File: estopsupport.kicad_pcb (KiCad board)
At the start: 2 copper layers, 65 x 35 mm, 23 parts, among them J1 ESTOP1, J2 ESTOP2, J3 CONTACTOR, J4 TAP_ESTOP, J5 5V_IN, J6 PWR, U1 PC817, U2 BTS6163D

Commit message: fix: shunt resistor value changed to datasheet recommendation
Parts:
- R4: value 10k -> 1k
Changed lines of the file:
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@@
 			)
 		)
-		(property "Value" "10k"
+		(property "Value" "1k"
 			(at 3.81 1.92 270)
 			(layer "F.Fab")

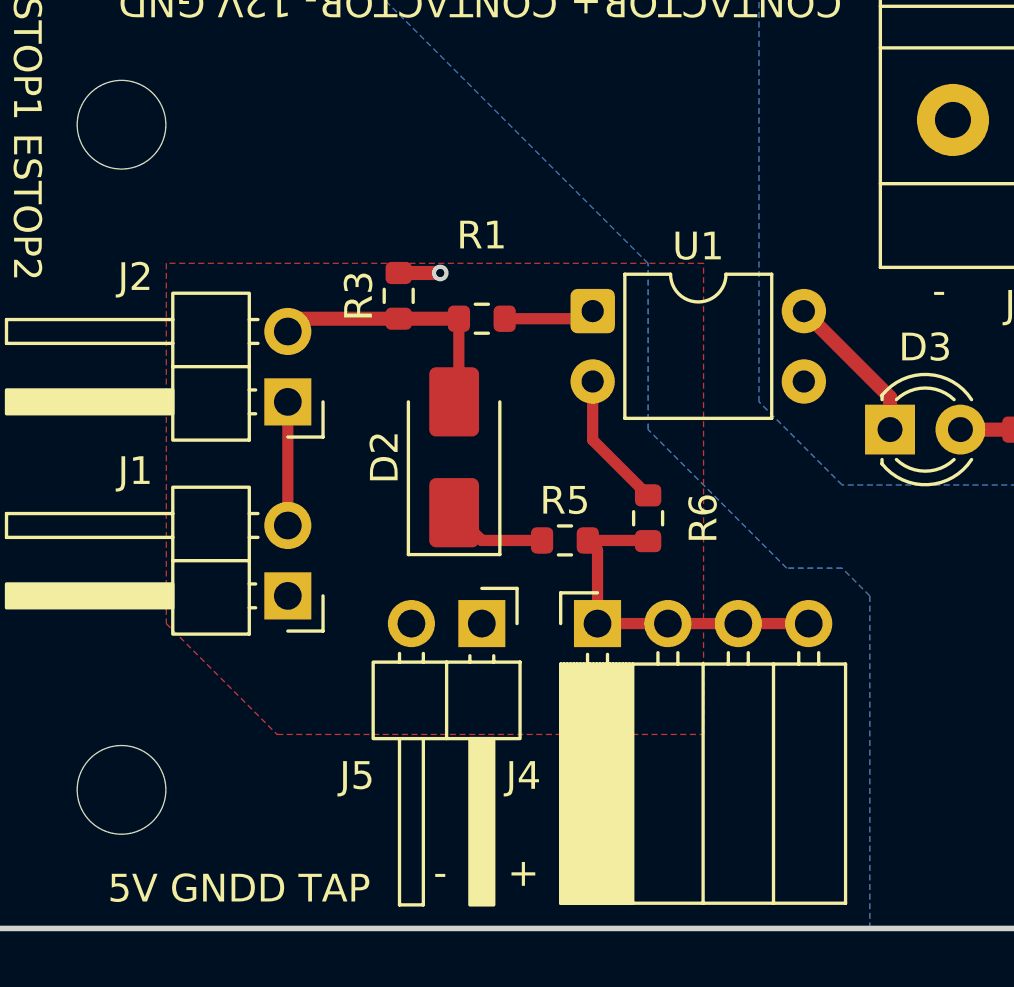
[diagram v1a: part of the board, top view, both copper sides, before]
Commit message: feat: started BOM, added ground lines to tap
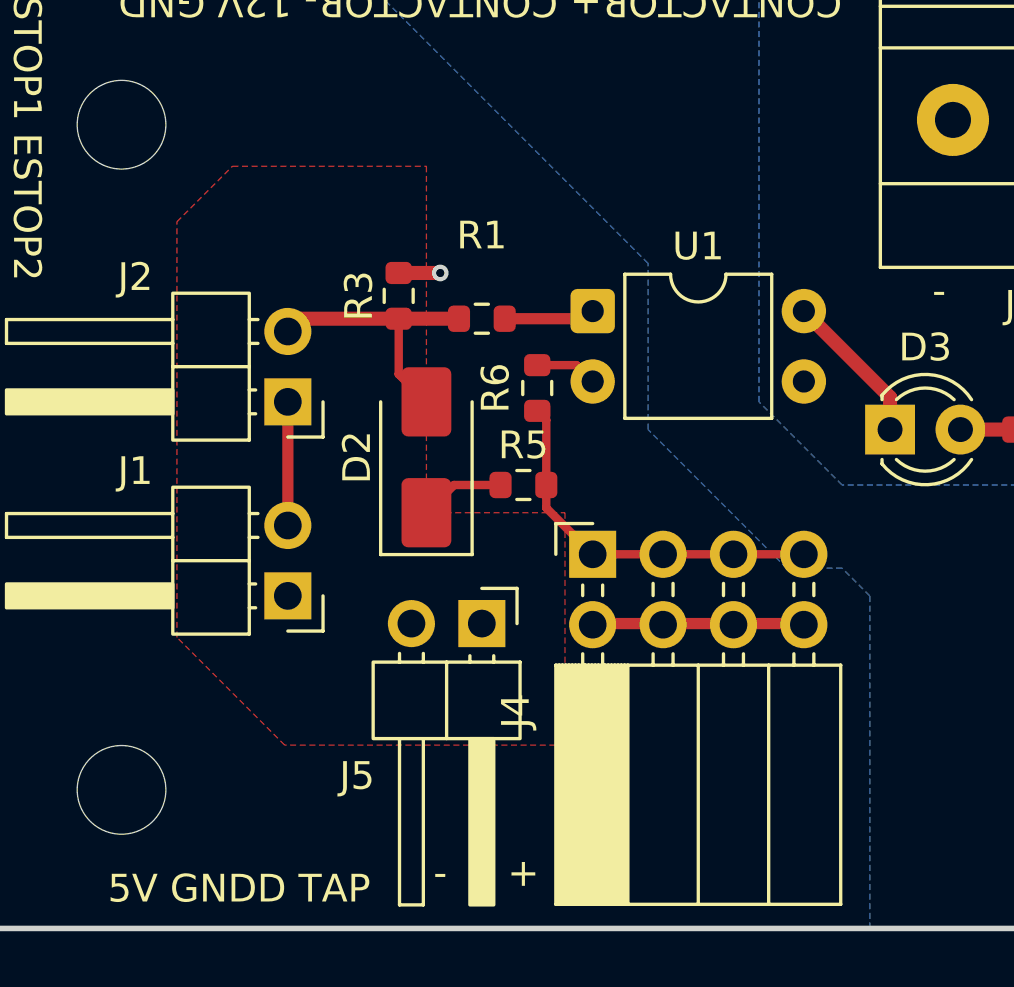
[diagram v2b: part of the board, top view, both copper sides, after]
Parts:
- J4: footprint Connector_PinSocket_2.54mm:PinSocket_1x04_P2.54mm_Horizontal -> Connector_PinSocket_2.54mm:PinSocket_2x04_P2.54mm_Horizontal
- R2: value 6.2k -> 1.6k
- moved R6 6.17 mm to (55.0, 46.8)
- moved J4 2.51 mm to (57.0, 52.8)
- moved R5 2.50 mm to (54.5, 50.3)
- moved D2 1.00 mm to (51.0, 49.3)
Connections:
- J4 pad 2: Net-(J4-Pin_1) -> GNDD
- J4 pad 4: Net-(J4-Pin_1) -> GNDD
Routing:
- net GNDD: track 6.44 -> 11.6 mm
- net Net-(J4-Pin_1): track 13.0 -> 13.6 mm
- net Net-(D2-K): track 3.59 -> 3.09 mm

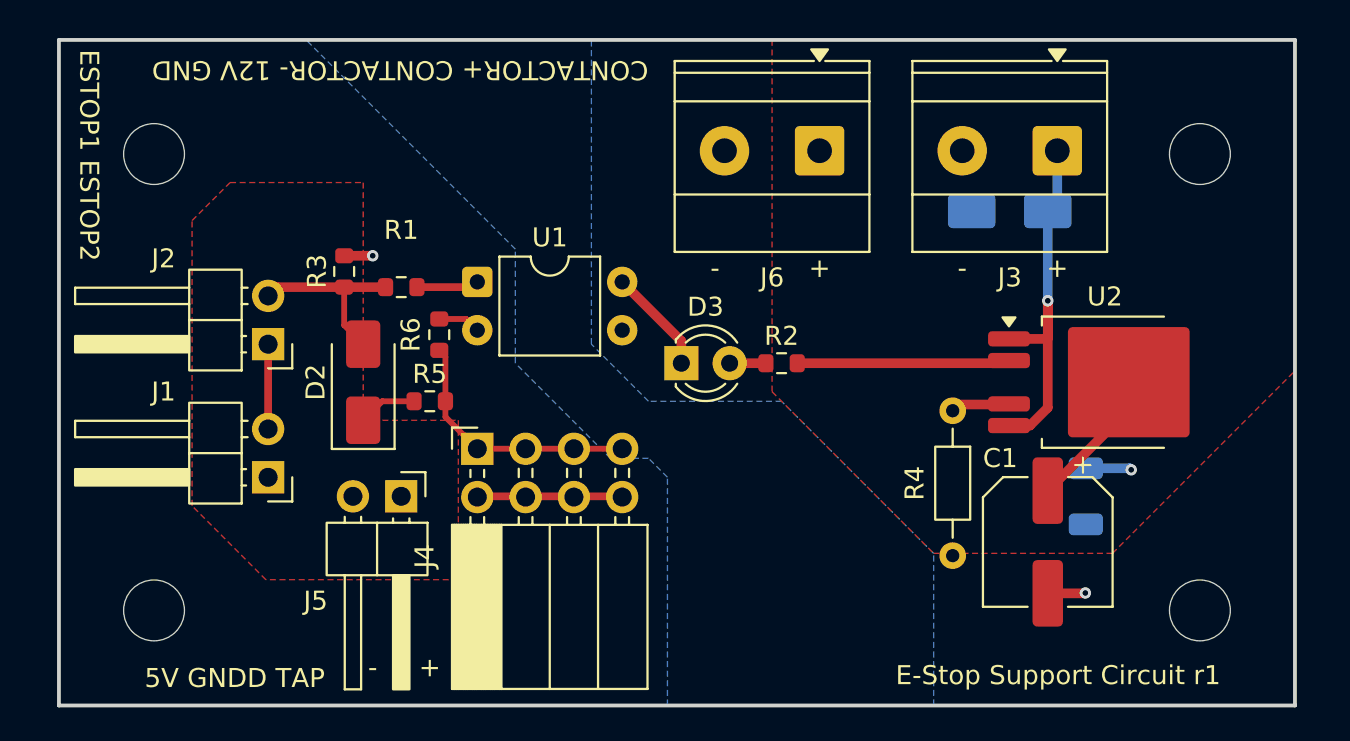
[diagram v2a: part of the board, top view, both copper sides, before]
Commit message: feat: change to use battery voltage directly for powering the coil
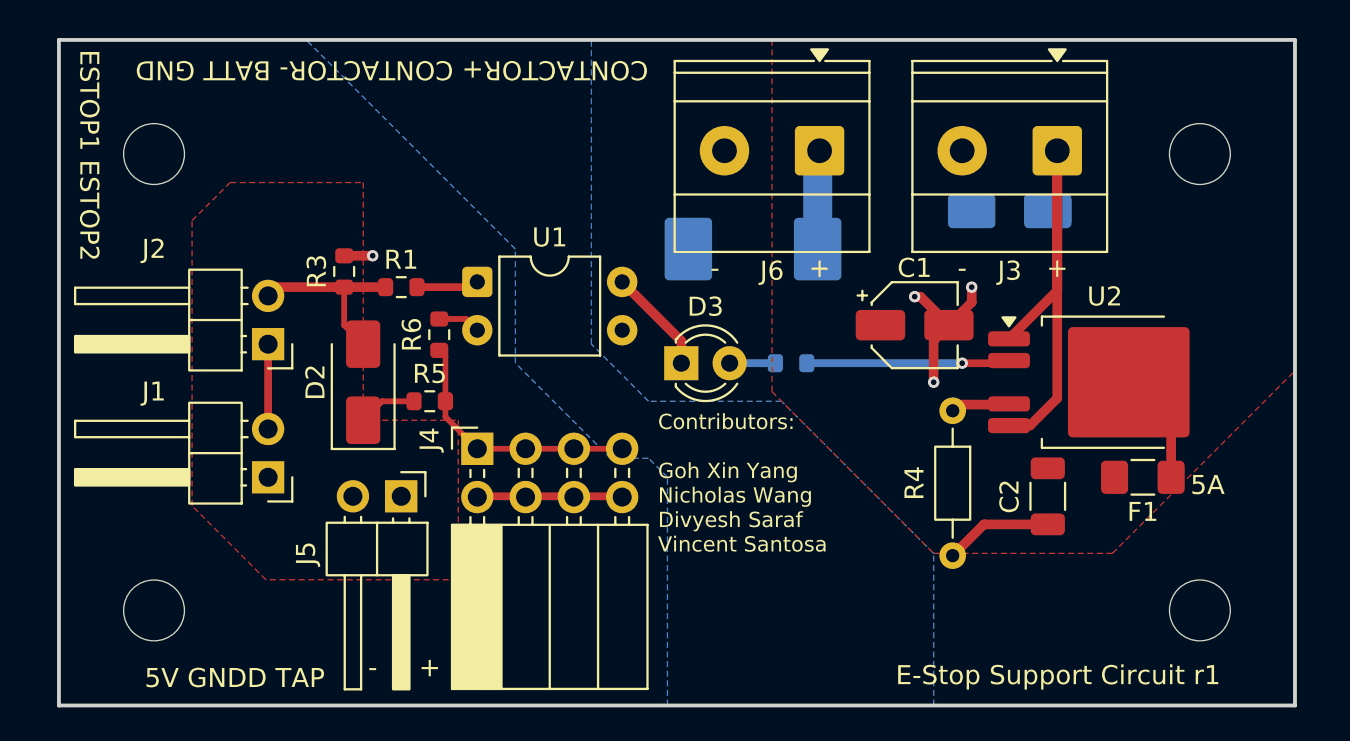
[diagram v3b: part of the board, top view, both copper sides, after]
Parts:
- added D4: SMCJ22A, Diode_SMD:D_SMC, B.Cu at (71.5, 42.3)
- added F1: Fuse, Fuse:Fuse_1206_3216Metric_Pad1.42x1.75mm_HandSolder, F.Cu at (92.0, 54.3)
- C1: value 100u -> 22u; footprint Capacitor_SMD:CP_Elec_6.3x7.7 -> Capacitor_SMD:CP_Elec_4x5.4
- C2: moved to F.Cu
- R2: moved to B.Cu
- R5: value 3.3k -> 4.3k
- moved C1 13.4 mm to (80.0, 46.3), turned to 0 degrees
- moved C2 2.00 mm to (87.0, 55.3)
- moved R2 0.50 mm to (73.5, 48.3)
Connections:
- C1 pad 1: +12V -> +BATT
- C2 pad 1: +12V -> +BATT
- J6 pad 1: +12V -> +BATT
- U2 pad 3: +12V -> Net-(U2-Vbb)
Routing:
- net GND: track 1.98 -> 13.9 mm, vias 1 -> 3
- net Net-(D1-K): track 20.2 -> 30.5 mm, vias 1 -> 0
- net +12V: track 9.89 -> 0.00 mm, vias 1 -> 0
- net Net-(U2-Vbb): track 0.00 -> 5.92 mm
- net +BATT: track 0.00 -> 4.21 mm
- net Net-(D3-A): track 1.90 -> 2.41 mm
- net Net-(U2-IN): track 11.3 -> 10.8 mm, vias 0 -> 1
- added copper zone on F.Cu, net +BATT
- removed copper zone on F.Cu, net +12V
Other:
- board text added: "5A"
- board text added: "CONTACTOR+ CONTACTOR- BATT GND"
- board text added: "Contributors: Goh Xin Yang Nicholas Wang Divyesh Saraf Vincent Santosa"
- board text removed: "CONTACTOR+ CONTACTOR- 12V GND"

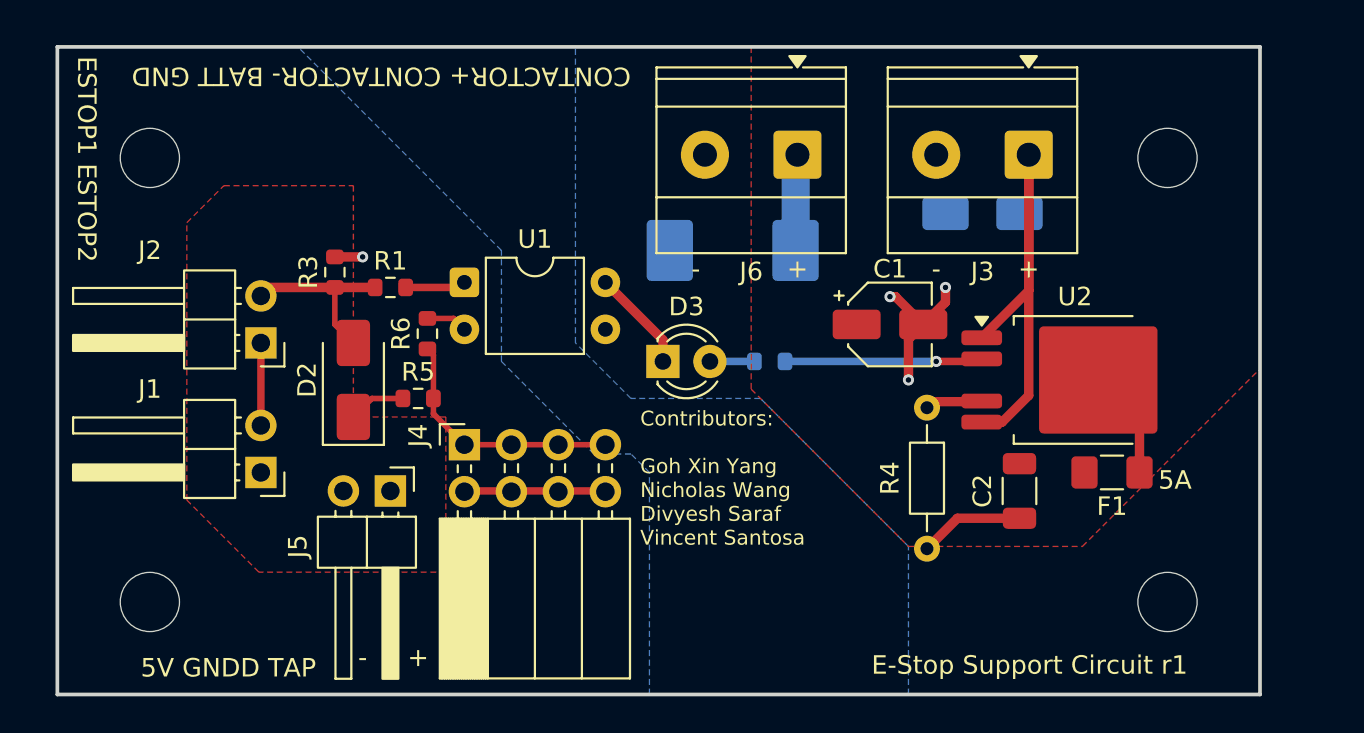
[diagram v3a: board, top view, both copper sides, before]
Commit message: feat: include logo properly, reroute to use capacitors properly, add fuse
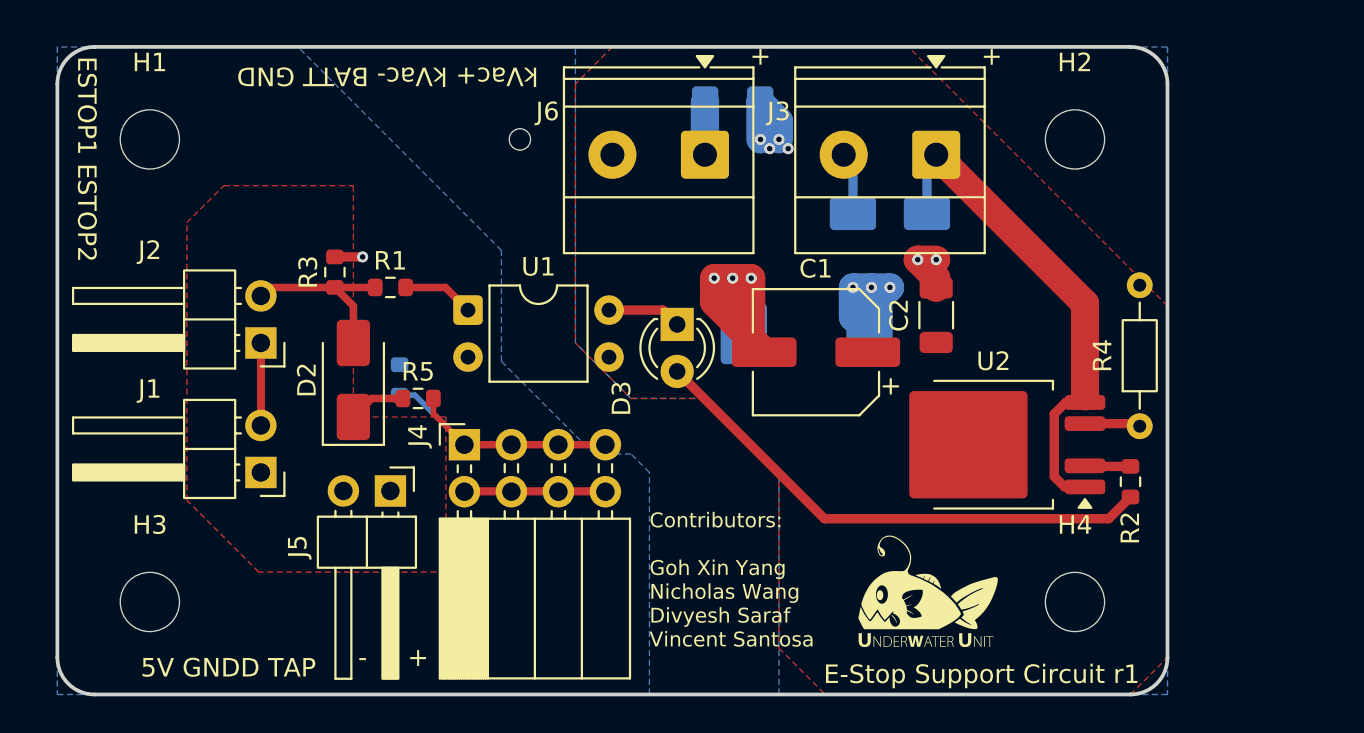
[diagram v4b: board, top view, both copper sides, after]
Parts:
- added G***: LOGO, graphics:uwu-logo, F.Cu at (82.0, 60.8)
- added REF**: ToolingHole_1.152mm, MountingHole:ToolingHole_1.152mm, F.Cu at (60.0, 36.3)
- C1: value 22u -> 47u; footprint Capacitor_SMD:CP_Elec_4x5.4 -> Capacitor_SMD:CP_Elec_6.3x5.4
- F1: value Fuse -> 5A; moved to B.Cu
- R2: moved to F.Cu
- R6: moved to B.Cu
- moved F1 28.6 mm to (71.5, 34.3), turned to 0 degrees
- moved R2 20.6 mm to (93.0, 54.8), turned to 90 degrees
- moved R4 11.5 mm to (93.5, 51.8), turned to 90 degrees
- moved C2 10.5 mm to (82.5, 45.8), turned to 90 degrees
- moved D4 6.02 mm to (75.5, 46.8)
- moved U2 5.70 mm to (85.5, 52.8), turned to 180 degrees
- moved H2 5.10 mm to (90.0, 36.3)
- moved D1 5.00 mm to (80.0, 40.3)
- moved H4 5.00 mm to (90.0, 61.3)
- moved J3 5.00 mm to (82.5, 37.1)
- moved J6 5.00 mm to (70.0, 37.1)
- moved C1 4.27 mm to (76.0, 47.8), turned to 180 degrees
- moved R6 2.92 mm to (53.5, 49.3)
- moved D3 2.14 mm to (68.5, 46.3), turned to -90 degrees
- moved U1 1.51 mm to (57.2, 45.5)
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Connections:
- F1 pad 1: Net-(U2-Vbb) -> Net-(J6-Pin_1)
- J6 pad 1: +BATT -> Net-(J6-Pin_1)
- U2 pad 3: Net-(U2-Vbb) -> +BATT
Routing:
- net Net-(D3-A): track 2.41 -> 28.3 mm
- net +BATT: track 4.21 -> 14.8 mm, vias 0 -> 7
- net Net-(J4-Pin_1): track 13.6 -> 23.0 mm
- net Net-(U2-IN): track 10.8 -> 2.47 mm, vias 1 -> 0
- net GND: track 13.9 -> 21.7 mm, vias 3 -> 5
- net Net-(U2-Vbb): track 5.92 -> 0.00 mm
- net GNDD: track 11.6 -> 16.7 mm
- net Net-(J1-Pin_2): track 4.46 -> 8.92 mm
- net Net-(D1-K): track 30.5 -> 26.3 mm
- net Net-(J6-Pin_1): track 0.00 -> 2.83 mm
- net Net-(D3-K): track 5.56 -> 4.01 mm
- net Net-(R1-Pad2): track 3.29 -> 3.88 mm
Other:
- board size 65 x 35 mm -> 60 x 35 mm
- board text added: "kVac+ kVac- BATT GND"
- board text removed: "CONTACTOR+ CONTACTOR- BATT GND"

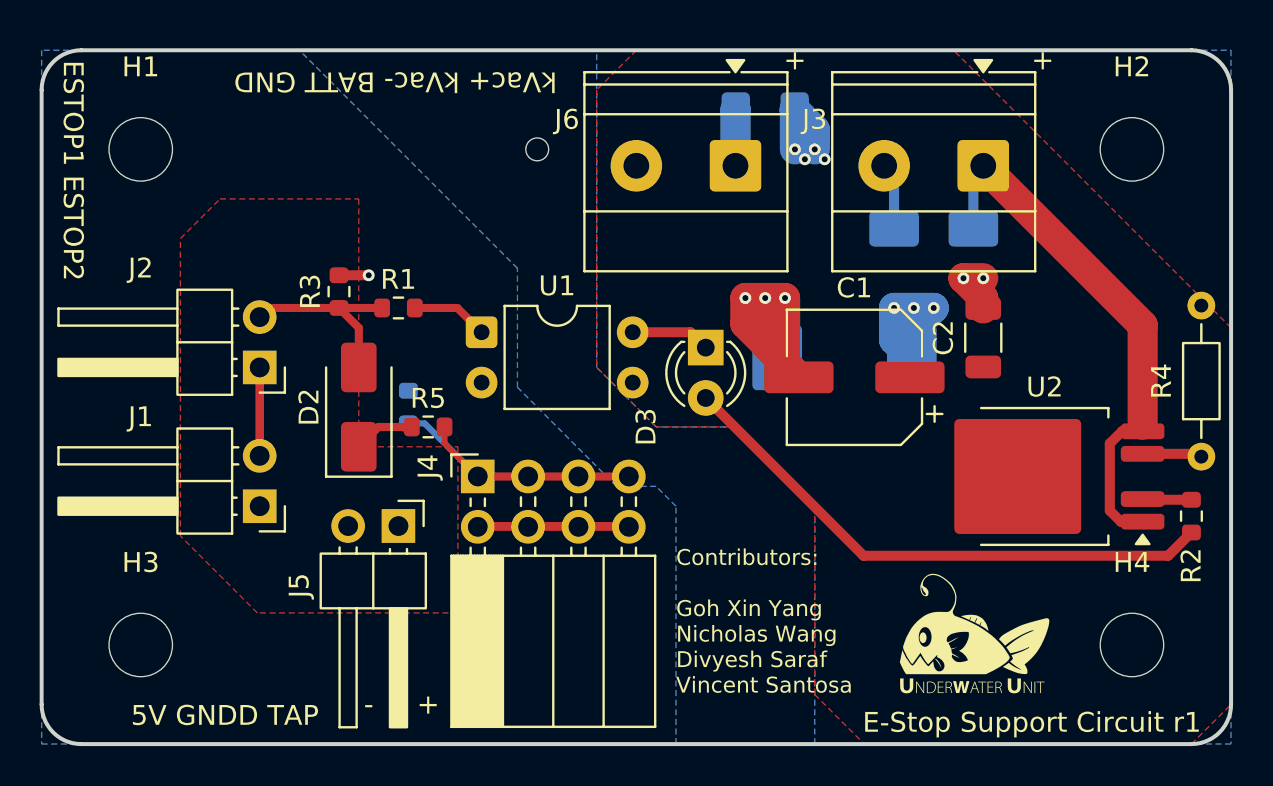
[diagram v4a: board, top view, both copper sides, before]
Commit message: fix: remove unneeded flyback for kilovac major rearrangement
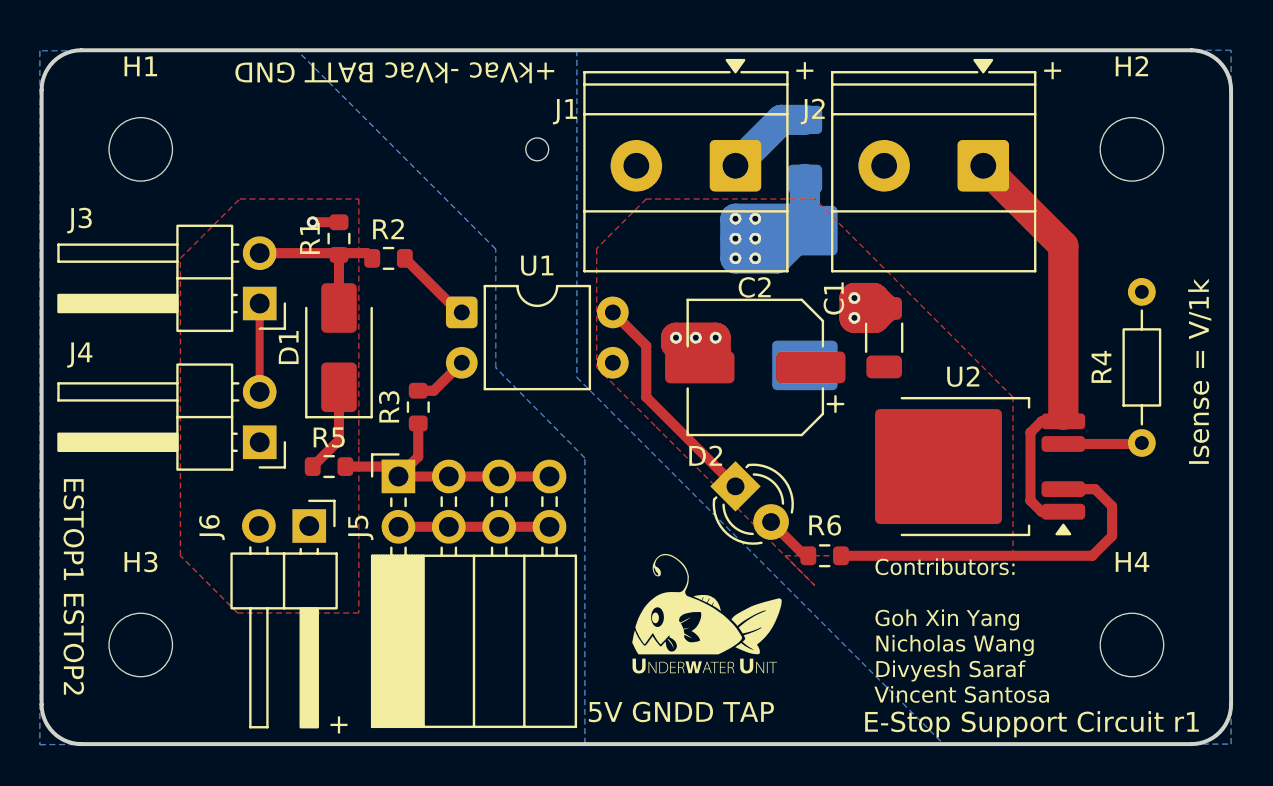
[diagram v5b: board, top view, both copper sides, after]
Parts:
- removed the D1 at (80.0, 40.3)
- R3: renamed from R6; moved to F.Cu
- moved R6 18.6 mm to (74.5, 56.8), turned to 0 degrees
- moved G*** 13.5 mm to (68.5, 59.8)
- moved D2 7.16 mm to (70.0, 53.3), turned to -45 degrees
- moved R5 5.39 mm to (49.5, 52.3)
- moved C2 5.02 mm to (71.0, 47.3)
- moved C1 5.00 mm to (77.5, 45.8)
- moved J6 4.50 mm to (48.5, 55.3)
- moved U2 4.03 mm to (81.5, 52.3)
- moved J5 4.00 mm to (53.0, 52.8)
- moved D3 3.61 mm to (73.5, 43.8), turned to -90 degrees
- moved J3 3.23 mm to (46.0, 44.0)
- moved J4 3.23 mm to (46.0, 51.0)
- moved D1 3.16 mm to (50.0, 46.3)
- moved R4 3.08 mm to (90.5, 51.1)
- moved F1 2.83 mm to (73.5, 36.3), turned to -90 degrees
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- renumbered C2 to C1, C1 to C2, D2 to D1, D3 to D2, D4 to D3, J6 to J1, J3 to J2, J2 to J3, J1 to J4, J4 to J5, J5 to J6, R3 to R1, R1 to R2, R2 to R6
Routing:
- net Net-(D2-A): track 28.3 -> 2.41 mm
- net Net-(U2-IN): track 2.47 -> 18.4 mm
- net GND: track 21.7 -> 10.2 mm
- net Net-(J5-Pin_1): track 23.0 -> 12.9 mm
- net Net-(D2-K): track 4.01 -> 11.3 mm
- net GNDD: track 16.7 -> 11.7 mm
- net Net-(J2-Pin_1): track 26.3 -> 21.5 mm
- net Net-(J3-Pin_1): track 8.92 -> 4.46 mm
- net Net-(J1-Pin_1): track 2.83 -> 4.46 mm
- net Net-(D1-K): track 3.09 -> 4.55 mm
- net Net-(D1-A): track 9.78 -> 8.46 mm
- net +BATT: track 14.8 -> 16.1 mm, vias 7 -> 6
- net Net-(U2-IS): track 3.02 -> 3.91 mm
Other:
- board text added: "+kVac -kVac BATT GND"
- board text added: "Isense = V/1k"
- board text removed: "-"
- board text removed: "kVac+ kVac- BATT GND"
